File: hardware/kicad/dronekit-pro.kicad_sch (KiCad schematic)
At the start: 30 parts, among them J101 3S–4S LiPo (11.1–16.8 V), Q101 AOD4185, U101 MP2307DN-LF-Z, U102 RT9013-33GB, U103 AP7361C-33E

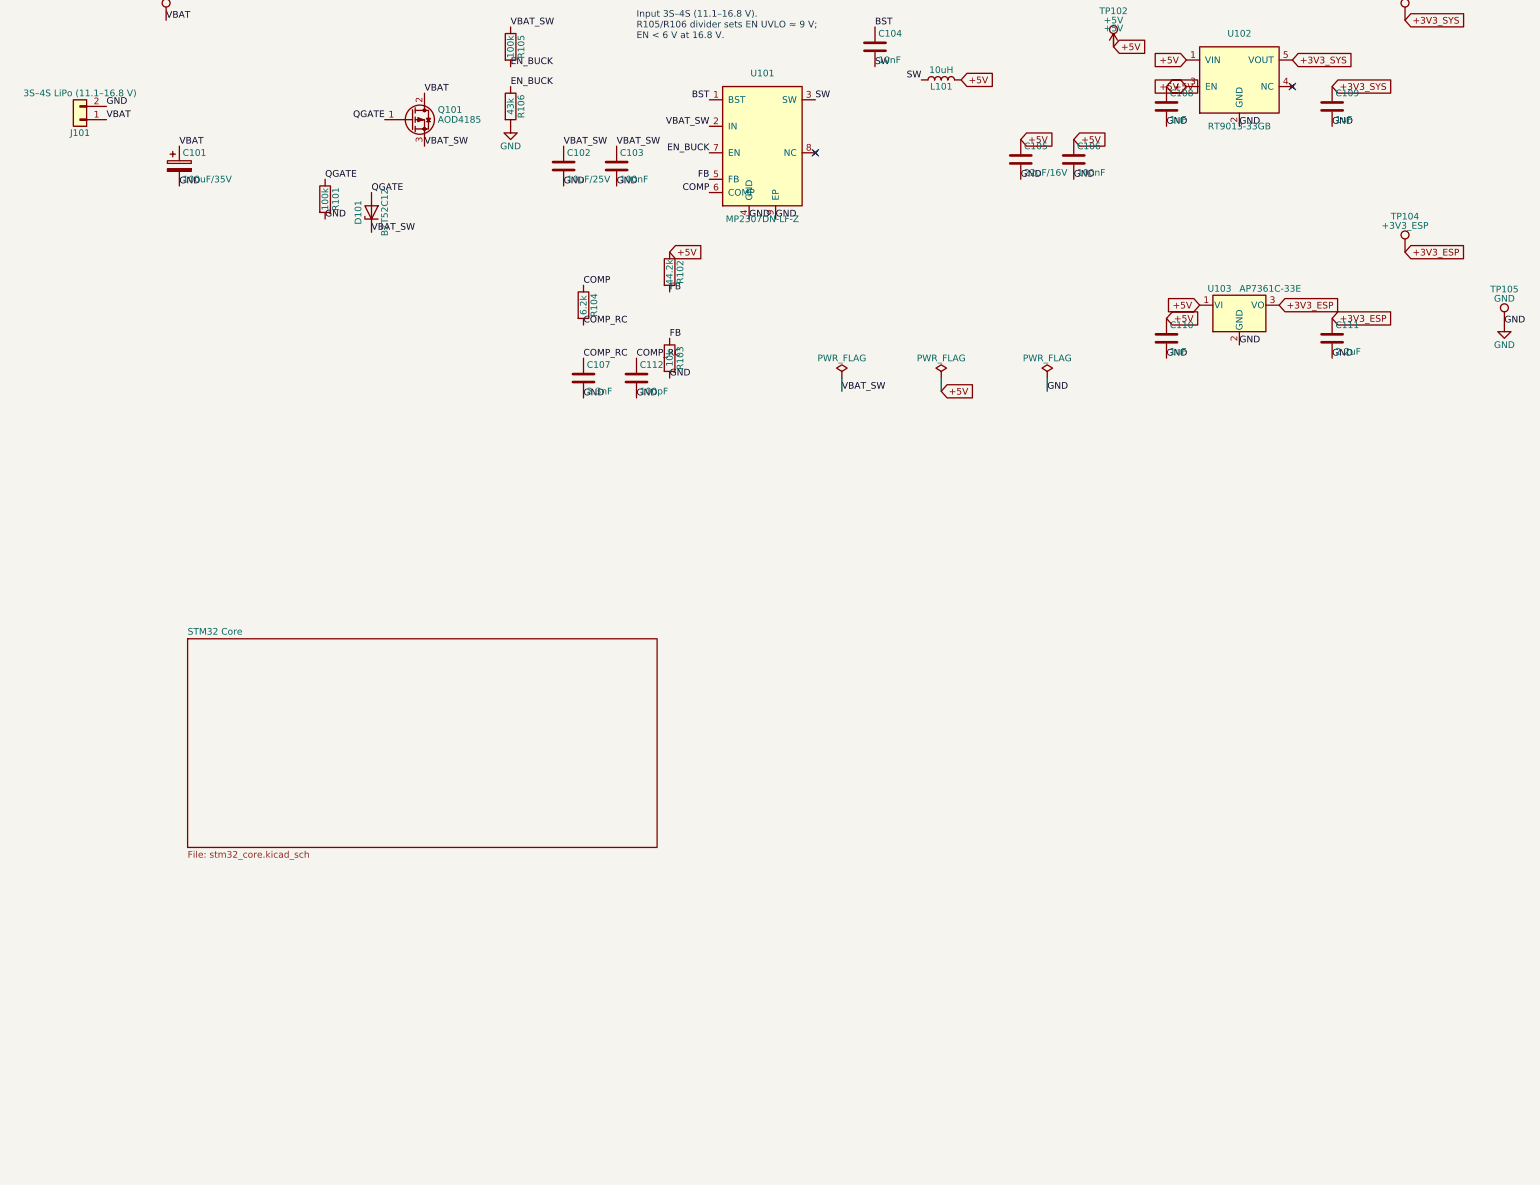
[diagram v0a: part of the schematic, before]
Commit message: Block 5: ESP32 sheet, mode switch, UART bridge, flash lines; PB12 series R; Block 1 GND to power symbols
Co-Authored-By: Claude Sonnet 5 <noreply@anthropic.com>
Claude-Session: https://claude.ai/code/session_01JDQYoFvbjRHNSgGtfc2pWo
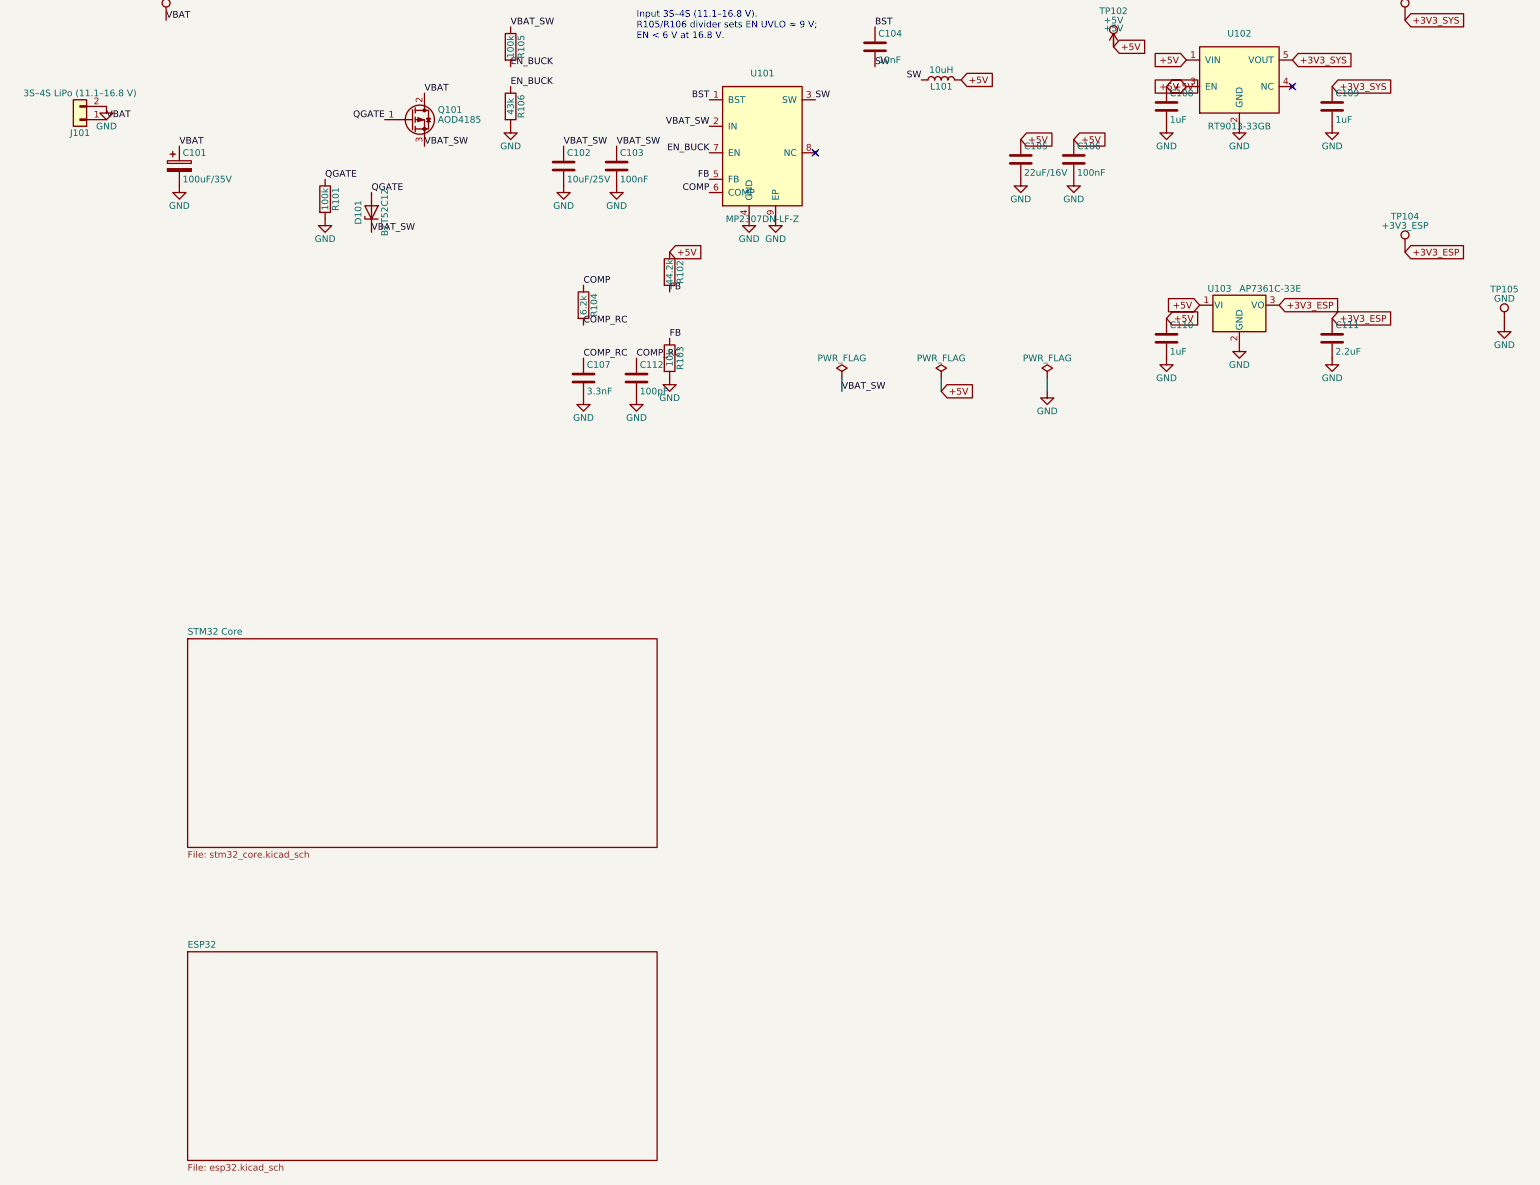
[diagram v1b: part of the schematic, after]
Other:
- added sheet ESP32 (esp32.kicad_sch)

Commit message: Block 3: ICM-42688-P IMU on SPI1
Also gitignore editor .history dir.

Co-Authored-By: Claude Sonnet 5 <noreply@anthropic.com>
Claude-Session: https://claude.ai/code/session_01JDQYoFvbjRHNSgGtfc2pWo
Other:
- added sheet IMU (imu.kicad_sch)
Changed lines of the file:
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@@
 		)
 	)
+	(sheet
+    (at 60 330)
+    (size 90 40)
+    (fields_autoplaced yes)
+    (stroke (width 0.1524) (type solid))
+    (fill (color 0 0 0 0.0))
+    (property "Sheetname" "IMU"
+      (at 60 329.365 0)
+      (effects (font (size 1.27 1.27)) (justify left bottom))
+    )
+    (property "Sheetfile" "imu.kicad_sch"
+      (at 60 370.635 0)
+      (effects (font (size 1.27 1.27)) (justify left top))
+    )
+    (instances
+      (project "dronekit-pro"
+        (path "/8ff649ce-ea17-45ea-9d2f-8e238e021cf9" (page "4"))
+      )
+    )
+  )
 )

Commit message: Block 4: DPS368 baro + W25Q128 flash; drop onboard SPI-ELRS, flash on SPI3/PA15, RX on UART3
Co-Authored-By: Claude Sonnet 5 <noreply@anthropic.com>
Claude-Session: https://claude.ai/code/session_01JDQYoFvbjRHNSgGtfc2pWo
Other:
- added sheet Baro + Flash (baro_flash.kicad_sch)
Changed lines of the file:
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@@
+    )
+  )
+	(sheet
+    (at 60 390)
+    (size 90 40)
+    (fields_autoplaced yes)
+    (stroke (width 0.1524) (type solid))
+    (fill (color 0 0 0 0.0))
+    (property "Sheetname" "Baro + Flash"
+      (at 60 389.365 0)
+      (effects (font (size 1.27 1.27)) (justify left bottom))
+    )
+    (property "Sheetfile" "baro_flash.kicad_sch"
+      (at 60 430.635 0)
+      (effects (font (size 1.27 1.27)) (justify left top))
+    )
+    (instances
+      (project "dronekit-pro"
+        (path "/8ff649ce-ea17-45ea-9d2f-8e238e021cf9" (page "5"))
+      )
     )
   )

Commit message: Block 6: motors sheet, 4in1 ESC connector, current-sense RC, J602 DNP; promote Block 1 VBAT labels to global
Co-Authored-By: Claude Sonnet 5 <noreply@anthropic.com>
Claude-Session: https://claude.ai/code/session_0171uwNh8K8uwZuWio9f35u1
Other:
- added sheet Motors (motors.kicad_sch)
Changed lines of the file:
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@@
 		)
 	)
-	(label "VBAT"
-		(at 44.45 110.49 0)
-		(effects
-			(font
-				(size 1.27 1.27)
-			)
-			(justify left bottom)
-		)
-	)
-	(label "VBAT"
-		(at 58.42 115.57 0)
-		(effects
-			(font
-				(size 1.27 1.27)
-			)
-			(justify left bottom)
-		)
-	)
-	(label "VBAT"
-		(at 55.88 91.44 0)
-		(effects
-			(font
-				(size 1.27 1.27)
-			)
-			(justify left bottom)
-		)
-	)
-	(label "VBAT"
-		(at 105.41 105.41 0)
-		(effects
-			(font
-				(size 1.27 1.27)
-			)
-			(justify left bottom)
-		)
-	)
 	(label "VBAT_SW"
 		(at 105.41 115.57 0)
@@
 		)
 	)
+	(global_label "VBAT"
+		(shape input)
+		(at 44.45 110.49 0)
+		(effects
+			(font
+				(size 1.27 1.27)
+			)
+			(justify left)
+		)
+	)
+	(global_label "VBAT"
+		(shape input)
+		(at 58.42 115.57 0)
+		(effects
+			(font
+				(size 1.27 1.27)
+			)
+			(justify left)
+		)
+	)
+	(global_label "VBAT"
+		(shape input)
+		(at 55.88 91.44 0)
+		(effects
+			(font
+				(size 1.27 1.27)
+			)
+			(justify left)
+		)
+	)
+	(global_label "VBAT"
+		(shape input)
+		(at 105.41 105.41 0)
+		(effects
+			(font
+				(size 1.27 1.27)
+			)
+			(justify left)
+		)
+	)
 	(sheet
 		(at 60 210)
@@
 		)
 	)
+	(sheet
+		(at 60 330)
+		(size 90 40)
+		(fields_autoplaced)
+		(stroke
+			(width 0.1524)
+			(type solid)
+		)
+		(fill
+			(color 0 0 0 0.0)
+		)
+		(property "Sheetname" "IMU"
+			(at 60 329.365 0)
+			(effects
+				(font
+					(size 1.27 1.27)
+				)
+				(justify left bottom)
+			)
+		)
+		(property "Sheetfile" "imu.kicad_sch"
+			(at 60 370.635 0)
+			(effects
+				(font
+					(size 1.27 1.27)
+				)
+				(justify left top)
+			)
+		)
+		(instances
+			(project "dronekit-pro"
+				(path "/8ff649ce-ea17-45ea-9d2f-8e238e021cf9"
+					(page "4")
+				)
+			)
+		)
+	)
+	(sheet
+		(at 60 390)
+		(size 90 40)
+		(fields_autoplaced)
+		(stroke
+			(width 0.1524)
+			(type solid)
+		)
+		(fill
+			(color 0 0 0 0.0)
+		)
+		(property "Sheetname" "Baro + Flash"
+			(at 60 389.365 0)
+			(effects
+				(font
+					(size 1.27 1.27)
+				)
+				(justify left bottom)
+			)
+		)
+		(property "Sheetfile" "baro_flash.kicad_sch"
+			(at 60 430.635 0)
+			(effects
+				(font
+					(size 1.27 1.27)
+				)
+				(justify left top)
+			)
+		)
+		(instances
+			(project "dronekit-pro"
+				(path "/8ff649ce-ea17-45ea-9d2f-8e238e021cf9"
+					(page "5")
+				)
+			)
+		)
+	)
+	(sheet
+		(at 60 450)
+		(size 90 40)
+		(fields_autoplaced)
+		(stroke
+			(width 0.1524)
+			(type solid)
+		)
+		(fill
+			(color 0 0 0 0.0)
+		)
+		(property "Sheetname" "Motors"
+			(at 60 449.365 0)
+			(effects
+				(font
+					(size 1.27 1.27)
+				)
+				(justify left bottom)
+			)
+		)
+		(property "Sheetfile" "motors.kicad_sch"
+			(at 60 490.635 0)
+			(effects
+				(font
+					(size 1.27 1.27)
+				)
+				(justify left top)
+			)
+		)
+		(instances
+			(project "dronekit-pro"
+				(path "/8ff649ce-ea17-45ea-9d2f-8e238e021cf9"
+					(page "6")
+				)
+			)
+		)
+	)
 	(symbol
 		(lib_id "Connector_Generic:Conn_01x02")
@@
 		)
 	)
-	(sheet
-    (at 60 330)
-    (size 90 40)
-    (fields_autoplaced yes)
-    (stroke (width 0.1524) (type solid))
-    (fill (color 0 0 0 0.0))
-    (property "Sheetname" "IMU"
-      (at 60 329.365 0)
-      (effects (font (size 1.27 1.27)) (justify left bottom))
-    )
-    (property "Sheetfile" "imu.kicad_sch"
-      (at 60 370.635 0)
-      (effects (font (size 1.27 1.27)) (justify left top))
-    )
-    (instances
-      (project "dronekit-pro"
-        (path "/8ff649ce-ea17-45ea-9d2f-8e238e021cf9" (page "4"))
-      )
-    )
-  )
-	(sheet
-    (at 60 390)
-    (size 90 40)
-    (fields_autoplaced yes)
-    (stroke (width 0.1524) (type solid))
-    (fill (color 0 0 0 0.0))
-    (property "Sheetname" "Baro + Flash"
-      (at 60 389.365 0)
-      (effects (font (size 1.27 1.27)) (justify left bottom))
-    )
-    (property "Sheetfile" "baro_flash.kicad_sch"
-      (at 60 430.635 0)
-      (effects (font (size 1.27 1.27)) (justify left top))
-    )
-    (instances
-      (project "dronekit-pro"
-        (path "/8ff649ce-ea17-45ea-9d2f-8e238e021cf9" (page "5"))
-      )
-    )
-  )
 )

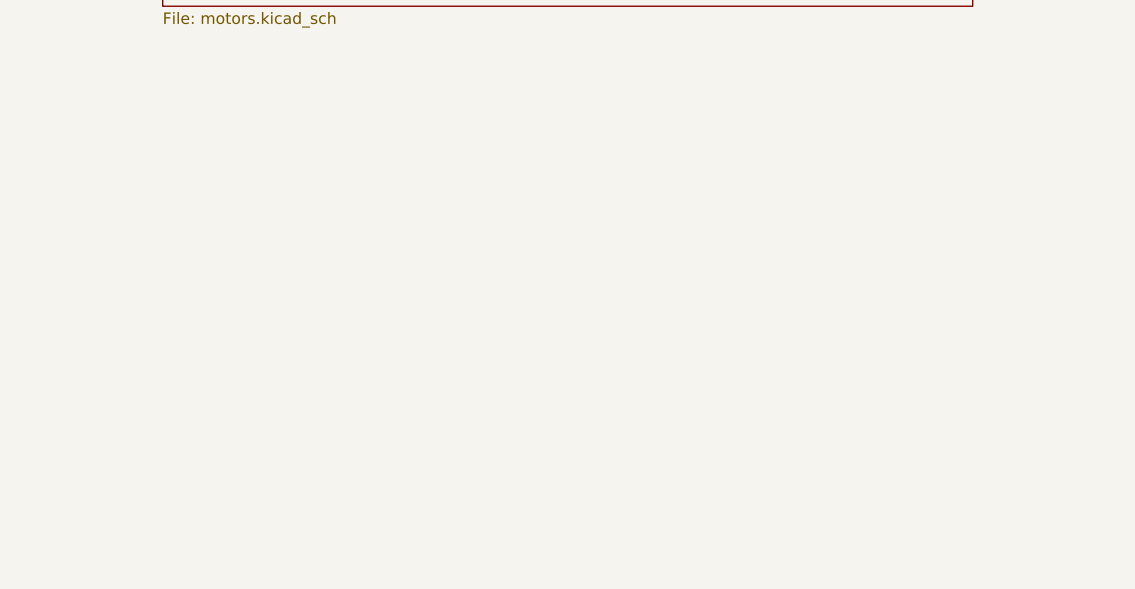
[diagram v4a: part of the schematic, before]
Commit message: Block 7: expansion connectors (RC, GPS, aux I2C, buzzer, LED)
- J701 CRSF on USART3, J702 GPS on USART2 (PA2/PA3)
- ESC_TLM assigned to UART5_RX (PD2), preserving USART2/4/6 as full pairs
- Buzzer low-side 2N7002 with flyback clamp; LED strip via 330R series
- Removes no-connect flags on PA2/PA3/PD2 in stm32_core
- LED_DATA drives WS2812 at 3V3 (VIH marginal) - see sheet note

Co-Authored-By: Claude Sonnet 5 <noreply@anthropic.com>
Claude-Session: https://claude.ai/code/session_0171uwNh8K8uwZuWio9f35u1
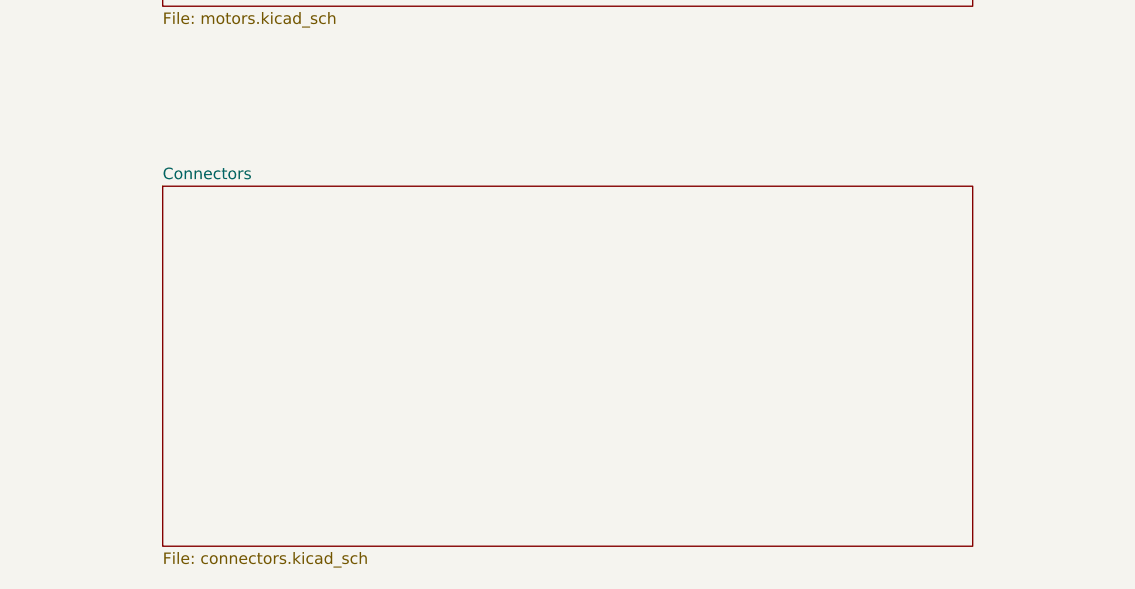
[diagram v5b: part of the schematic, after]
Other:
- added sheet Connectors (connectors.kicad_sch)
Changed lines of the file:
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@@
 		)
 	)
+	(sheet
+    (at 60 510)
+    (size 90 40)
+    (fields_autoplaced yes)
+    (stroke (width 0.1524) (type solid))
+    (fill (color 0 0 0 0.0))
+    (property "Sheetname" "Connectors"
+      (at 60 509.365 0)
+      (effects (font (size 1.27 1.27)) (justify left bottom))
+    )
+    (property "Sheetfile" "connectors.kicad_sch"
+      (at 60 550.635 0)
+      (effects (font (size 1.27 1.27)) (justify left top))
+    )
+    (instances
+      (project "dronekit-pro"
+        (path "/8ff649ce-ea17-45ea-9d2f-8e238e021cf9" (page "7"))
+      )
+    )
+  )
 )

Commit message: Block 8: USB-C, dual ideal-diode OR, VBAT sense
- J801 USB-C 16P, USBLC6-2SC6 ESD array, 5.1k CC pull-downs (UFP, no PD)
- U802/U803 LM66100 ideal diodes OR VBUS and +5V_BUCK onto +5V (~48 mV drop)
- Buck output split to +5V_BUCK; FB divider moved to its own output, removing
  the cross-coupling between buck regulation and the USB source
- Fixes MP2307 back-feed via high-side body diode when running on USB alone
- VBAT sense 100k/15k -> PC1, 146 uA quiescent, needs >=84-cycle ADC sample time
- ERC power_output x power_output downgraded to Warning for the sanctioned
  U802/U803 OR node only; see design-rule note

Schematic complete: blocks 1-8, ERC 0 errors / 3 known warnings.

Co-Authored-By: Claude Sonnet 5 <noreply@anthropic.com>
Claude-Session: https://claude.ai/code/session_0171uwNh8K8uwZuWio9f35u1
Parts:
- added U803: LM66100DCKR, Package_TO_SOT_SMD:SOT-363_SC-70-6, symbol Power_Management:LM66100DCK
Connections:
- net +5V: now also U803.3 (~{CE}), U803.6 (VOUT); no longer C105.1, C106.1, L101.2, R102.1
- net GND: now also U803.2 (GND)
- new net +5V_BUCK: C105.1, C106.1, L101.2, R102.1, U803.1 (VIN)
- no-connect marks 2 -> 4
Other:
- added sheet USB + Power sense (usb_power.kicad_sch)
- note added: "Buck-side OR-ing ideal diode (U803, LM66100DCKR): MP2307 output = +5V_BUCK (L101 / C105 / C106). FB (R102/R103) senses +5V_BUCK, so the buck regulates ITS OWN output to 5.0 V (no cross-coupling to the USB source). U803: VIN=+5V_BUCK, VOUT=+5V, CE tied to VOUT, GND to GND -> reverse-current-blocking ideal diode, ~48 mV drop at 0.5 A. Why: MP2307 is synchronous; its integrated high-side FET body di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"
